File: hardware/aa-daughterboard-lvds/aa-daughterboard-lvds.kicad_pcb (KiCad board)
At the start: 4 copper layers, 112 parts, among them CN1 Barrel_Jack, CN10 6P6C, CN11 6P6C, CN12 6P6C, CN13 6P6C, CN14 Conn_01x08, CN15 Conn_01x08, CN16 Conn_01x08, CN17 8P8C, CN18 8P8C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

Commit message: First run at aa-daughterboard (current loop version), plus WIP
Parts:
- removed C10, C11, C18, C19, C20: 1u, Capacitor_SMD:C_0805_2012Metric
- C12, C13, C14, C6, C7: value 1u -> 0.1u; footprint Capacitor_SMD:C_0805_2012Metric -> Capacitor_SMD:C_0603_1608Metric
- CN10, CN11, CN12, CN13, CN5: footprint aa-daughterboard-lvds:RJ25_Amphenol_90520 -> aa-daughterboard-lvds:6P6C_Assmann_A-2014-1-4
- CN17, CN18, CN19: footprint aa-daughterboard-lvds:RJ25_Assmann_A-2014-2S-4-N-R -> aa-daughterboard-lvds:8P8C_Assmann_A-2014-2S-4
- D6: moved to B.Cu
- moved C15 343.0 mm to (-12.2, 302.4)
- moved C12 343.0 mm to (-12.7, 308.1)
- moved C6 324.4 mm to (71.7, 300.0)
- moved CN15 320.7 mm to (-0.51, 227.8)
- moved CN16 320.2 mm to (-32.5, 202.4)
- moved CN14 320.0 mm to (6.60, 281.7)
- moved U7 309.0 mm to (-12.5, 238.6)
- moved U4 307.5 mm to (70.6, 290.8)
- moved CN5 292.7 mm to (19.1, 74.7), turned to 270 degrees
- moved TP8 290.1 mm to (140.2, 129.0)
- moved D15 289.8 mm to (-5.08, 296.9)
- moved D14 284.6 mm to (-3.81, 285.0)
- moved D16 283.8 mm to (-43.6, 241.0)
- moved C16 274.9 mm to (-43.3, 233.2)
- moved TP7 268.8 mm to (126.7, 130.6)
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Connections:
- CN10 pad 1: GND -> +5V
- CN11 pad 1: GND -> +5V
- CN12 pad 1: GND -> +5V
- CN13 pad 1: GND -> +5V
- CN17 pad 1: Net-(CN14-Pad7) -> Net-(CN14-Pad6)
- CN17 pad 2: Net-(CN14-Pad8) -> Net-(CN14-Pad5)
- CN17 pad 3: Net-(CN14-Pad3) -> Net-(CN14-Pad4)
- CN17 pad 4: Net-(CN14-Pad4) -> Net-(CN14-Pad2)
- CN17 pad 6: Net-(CN14-Pad2) -> Net-(CN14-Pad3)
- CN17 pad 7: Net-(CN14-Pad5) -> Net-(CN14-Pad8)
- CN17 pad 8: Net-(CN14-Pad6) -> Net-(CN14-Pad7)
- CN18 pad 1: Net-(CN15-Pad7) -> Net-(CN15-Pad6)
- CN18 pad 2: Net-(CN15-Pad8) -> Net-(CN15-Pad5)
- CN18 pad 3: Net-(CN15-Pad3) -> Net-(CN15-Pad4)
- CN18 pad 4: Net-(CN15-Pad4) -> Net-(CN15-Pad2)
- CN18 pad 6: Net-(CN15-Pad2) -> Net-(CN15-Pad3)
- CN18 pad 7: Net-(CN15-Pad5) -> Net-(CN15-Pad8)
- CN18 pad 8: Net-(CN15-Pad6) -> Net-(CN15-Pad7)
- CN19 pad 1: Net-(CN16-Pad7) -> Net-(CN16-Pad6)
- CN19 pad 2: Net-(CN16-Pad8) -> Net-(CN16-Pad5)
- CN19 pad 3: Net-(CN16-Pad3) -> Net-(CN16-Pad4)
- CN19 pad 4: Net-(CN16-Pad4) -> Net-(CN16-Pad2)
- CN19 pad 6: Net-(CN16-Pad2) -> Net-(CN16-Pad3)
- CN19 pad 7: Net-(CN16-Pad5) -> Net-(CN16-Pad8)
- CN19 pad 8: Net-(CN16-Pad6) -> Net-(CN16-Pad7)
- CN6 pad 1: Net-(CN10-Pad4) -> Net-(CN10-Pad3)
- CN6 pad 2: Net-(CN10-Pad5) -> Net-(CN10-Pad4)
- CN6 pad 4: Net-(CN10-Pad3) -> Net-(CN10-Pad5)
- CN7 pad 1: Net-(CN11-Pad4) -> Net-(CN11-Pad3)
- CN7 pad 2: Net-(CN11-Pad5) -> Net-(CN11-Pad4)
- CN7 pad 4: Net-(CN11-Pad3) -> Net-(CN11-Pad5)
- CN8 pad 1: Net-(CN12-Pad4) -> Net-(CN12-Pad3)
- CN8 pad 2: Net-(CN12-Pad5) -> Net-(CN12-Pad4)
- CN8 pad 4: Net-(CN12-Pad3) -> Net-(CN12-Pad5)
- CN9 pad 1: Net-(CN13-Pad4) -> Net-(CN13-Pad3)
- CN9 pad 2: Net-(CN13-Pad5) -> Net-(CN13-Pad4)
- CN9 pad 4: Net-(CN13-Pad3) -> Net-(CN13-Pad5)
- D10 pad 3: Net-(CN10-Pad3) -> Net-(CN10-Pad5)
- D10 pad 4: Net-(CN10-Pad4) -> Net-(CN10-Pad3)
- D10 pad 6: Net-(CN10-Pad5) -> Net-(CN10-Pad4)
- D11 pad 3: Net-(CN11-Pad3) -> Net-(CN11-Pad5)
- D11 pad 4: Net-(CN11-Pad4) -> Net-(CN11-Pad3)
- D11 pad 6: Net-(CN11-Pad5) -> Net-(CN11-Pad4)
- D12 pad 3: Net-(CN12-Pad3) -> Net-(CN12-Pad5)
- D12 pad 4: Net-(CN12-Pad4) -> Net-(CN12-Pad3)
- D12 pad 6: Net-(CN12-Pad5) -> Net-(CN12-Pad4)
- D13 pad 3: Net-(CN13-Pad3) -> Net-(CN13-Pad5)
- D13 pad 4: Net-(CN13-Pad4) -> Net-(CN13-Pad3)
- D13 pad 6: Net-(CN13-Pad5) -> Net-(CN13-Pad4)
- R11 pad 1: Net-(D7-Pad1) -> GND
- R11 pad 2: GND -> Net-(D7-Pad1)
- R13 pad 1: Net-(D8-Pad1) -> GND
- R13 pad 2: GND -> Net-(D8-Pad1)
- R14 pad 1: Net-(D9-Pad1) -> GND
- R14 pad 2: GND -> Net-(D9-Pad1)
- R2 pad 1: Net-(D1-Pad1) -> GND
- R2 pad 2: GND -> Net-(D1-Pad1)
- R8 pad 1: Net-(D4-Pad1) -> GND
- R8 pad 2: GND -> Net-(D4-Pad1)
- R9 pad 1: Net-(D5-Pad1) -> GND
- R9 pad 2: GND -> Net-(D5-Pad1)
- U4 pad 10: Net-(CN11-Pad4) -> Net-(CN11-Pad3)
- U4 pad 11: Net-(CN11-Pad5) -> Net-(CN11-Pad4)
- U4 pad 13: Net-(CN11-Pad3) -> Net-(CN11-Pad5)
- U4 pad 2: Net-(CN10-Pad4) -> Net-(CN10-Pad3)
- U4 pad 3: Net-(CN10-Pad5) -> Net-(CN10-Pad4)
- U4 pad 5: Net-(CN10-Pad3) -> Net-(CN10-Pad5)
- U5 pad 10: Net-(CN13-Pad4) -> Net-(CN13-Pad3)
- U5 pad 11: Net-(CN13-Pad5) -> Net-(CN13-Pad4)
- U5 pad 13: Net-(CN13-Pad3) -> Net-(CN13-Pad5)
- U5 pad 2: Net-(CN12-Pad4) -> Net-(CN12-Pad3)
- U5 pad 3: Net-(CN12-Pad5) -> Net-(CN12-Pad4)
- U5 pad 5: Net-(CN12-Pad3) -> Net-(CN12-Pad5)

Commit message: Rough grouping of components done
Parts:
- added R16: 56, Resistor_SMD:R_0603_1608Metric, F.Cu at (86.1, 100.9)
- added R17: 56, Resistor_SMD:R_0603_1608Metric, F.Cu at (80.0, 100.8)
- added R18: 56, Resistor_SMD:R_0603_1608Metric, F.Cu at (79.2, 112.5)
- added R19: 56, Resistor_SMD:R_0603_1608Metric, F.Cu at (84.8, 112.5)
- added R20: 56, Resistor_SMD:R_0603_1608Metric, F.Cu at (84.8, 80.5)
- added R21: 56, Resistor_SMD:R_0603_1608Metric, F.Cu at (79.2, 80.5)
- added R22: 56, Resistor_SMD:R_0603_1608Metric, F.Cu at (78.0, 92.2)
- added R23: 56, Resistor_SMD:R_0603_1608Metric, F.Cu at (83.6, 92.2)
- added R24: 56, Resistor_SMD:R_0603_1608Metric, F.Cu at (84.3, 100.8)
- added R25: 56, Resistor_SMD:R_0603_1608Metric, F.Cu at (82.0, 100.8)
- added R26: 56, Resistor_SMD:R_0603_1608Metric, F.Cu at (81.0, 112.5)
- added R27: 56, Resistor_SMD:R_0603_1608Metric, F.Cu at (83.1, 112.5)
- added R28: 56, Resistor_SMD:R_0603_1608Metric, F.Cu at (83.1, 80.5)
- added R29: 56, Resistor_SMD:R_0603_1608Metric, F.Cu at (81.0, 80.5)
- added R30: 56, Resistor_SMD:R_0603_1608Metric, F.Cu at (79.8, 92.2)
- added R31: 56, Resistor_SMD:R_0603_1608Metric, F.Cu at (81.8, 92.2)
- added R32: 56, Resistor_SMD:R_0603_1608Metric, F.Cu at (84.6, 60.2)
- added R33: 56, Resistor_SMD:R_0603_1608Metric, F.Cu at (79.0, 60.2)
- added R34: 56, Resistor_SMD:R_0603_1608Metric, F.Cu at (78.0, 71.9)
- added R35: 56, Resistor_SMD:R_0603_1608Metric, F.Cu at (83.6, 71.9)
- added R36: 56, Resistor_SMD:R_0603_1608Metric, F.Cu at (64.5, 65.3)
- added R37: 56, Resistor_SMD:R_0603_1608Metric, F.Cu at (58.8, 65.3)
- added R38: 56, Resistor_SMD:R_0603_1608Metric, F.Cu at (57.7, 77.0)
- added R39: 56, Resistor_SMD:R_0603_1608Metric, F.Cu at (63.2, 77.0)
- added R40: 56, Resistor_SMD:R_0603_1608Metric, F.Cu at (64.5, 88.1)
- added R41: 56, Resistor_SMD:R_0603_1608Metric, F.Cu at (58.7, 88.1)
- added R42: 56, Resistor_SMD:R_0603_1608Metric, F.Cu at (57.7, 99.8)
- added R43: 56, Resistor_SMD:R_0603_1608Metric, F.Cu at (63.2, 99.8)
- added R44: 56, Resistor_SMD:R_0603_1608Metric, F.Cu at (82.8, 60.2)
- added R45: 56, Resistor_SMD:R_0603_1608Metric, F.Cu at (80.8, 60.2)
- added R46: 56, Resistor_SMD:R_0603_1608Metric, F.Cu at (79.8, 71.9)
- added R47: 56, Resistor_SMD:R_0603_1608Metric, F.Cu at (81.8, 71.9)
- added R48: 56, Resistor_SMD:R_0603_1608Metric, F.Cu at (62.7, 65.3)
- added R49: 56, Resistor_SMD:R_0603_1608Metric, F.Cu at (60.5, 65.3)
- added R50: 56, Resistor_SMD:R_0603_1608Metric, F.Cu at (59.4, 77.0)
- added R51: 56, Resistor_SMD:R_0603_1608Metric, F.Cu at (61.5, 77.0)
- added R52: 56, Resistor_SMD:R_0603_1608Metric, F.Cu at (62.7, 88.1)
- added R53: 56, Resistor_SMD:R_0603_1608Metric, F.Cu at (60.5, 88.1)
- added R54: 56, Resistor_SMD:R_0603_1608Metric, F.Cu at (59.4, 99.8)
- added R55: 56, Resistor_SMD:R_0603_1608Metric, F.Cu at (61.5, 99.8)
- C2, C8, C9, D10, D11, D12, D13: moved to B.Cu
- Q1: footprint Package_TO_SOT_THT:TO-220-3_Horizontal_TabDown -> Package_TO_SOT_THT:TO-220-3_Vertical
- moved CN17 293.5 mm to (169.7, 90.2)
- moved C15 287.3 mm to (174.2, 83.8), turned to 90 degrees
- moved D15 276.1 mm to (170.4, 83.8)
- moved D14 271.2 mm to (178.1, 83.8), turned to 180 degrees
- moved C12 255.8 mm to (85.6, 71.9), turned to 270 degrees
- moved CN14 254.3 mm to (184.9, 100.3), turned to 180 degrees
- moved D16 253.6 mm to (155.4, 83.8), turned to 180 degrees
- moved CN11 253.1 mm to (173.2, 59.2), turned to 0 degrees
- moved C16 245.5 mm to (151.6, 83.8), turned to 90 degrees
- moved U6 245.5 mm to (81.3, 66.0), turned to 270 degrees
- moved CN18 237.8 mm to (146.8, 90.2), turned to 0 degrees
- moved D11 234.4 mm to (156.5, 54.0), turned to 180 degrees
- moved CN10 232.0 mm to (155.4, 59.2)
- moved D17 229.9 mm to (147.8, 83.8), turned to 180 degrees
- moved C8 229.2 mm to (153.2, 54.0), turned to 270 degrees
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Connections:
- U4 pad 10: Net-(CN11-Pad3) -> Net-(R18-Pad1)
- U4 pad 11: Net-(CN11-Pad4) -> Net-(R26-Pad1)
- U4 pad 13: Net-(CN11-Pad5) -> Net-(R27-Pad1)
- U4 pad 14: Net-(CN11-Pad2) -> Net-(R19-Pad1)
- U4 pad 2: Net-(CN10-Pad3) -> Net-(R16-Pad1)
- U4 pad 3: Net-(CN10-Pad4) -> Net-(R24-Pad1)
- U4 pad 5: Net-(CN10-Pad5) -> Net-(R25-Pad1)
- U4 pad 6: Net-(CN10-Pad2) -> Net-(R17-Pad1)
- U5 pad 10: Net-(CN13-Pad3) -> Net-(R22-Pad1)
- U5 pad 11: Net-(CN13-Pad4) -> Net-(R30-Pad1)
- U5 pad 13: Net-(CN13-Pad5) -> Net-(R31-Pad1)
- U5 pad 14: Net-(CN13-Pad2) -> Net-(R23-Pad1)
- U5 pad 2: Net-(CN12-Pad3) -> Net-(R20-Pad1)
- U5 pad 3: Net-(CN12-Pad4) -> Net-(R28-Pad1)
- U5 pad 5: Net-(CN12-Pad5) -> Net-(R29-Pad1)
- U5 pad 6: Net-(CN12-Pad2) -> Net-(R21-Pad1)
- U6 pad 10: Net-(CN14-Pad5) -> Net-(R34-Pad1)
- U6 pad 11: Net-(CN14-Pad6) -> Net-(R46-Pad1)
- U6 pad 13: Net-(CN14-Pad8) -> Net-(R47-Pad1)
- U6 pad 14: Net-(CN14-Pad7) -> Net-(R35-Pad1)
- U6 pad 2: Net-(CN14-Pad1) -> Net-(R32-Pad1)
- U6 pad 3: Net-(CN14-Pad2) -> Net-(R44-Pad1)
- U6 pad 5: Net-(CN14-Pad4) -> Net-(R45-Pad1)
- U6 pad 6: Net-(CN14-Pad3) -> Net-(R33-Pad1)
- U7 pad 10: Net-(CN15-Pad5) -> Net-(R38-Pad1)
- U7 pad 11: Net-(CN15-Pad6) -> Net-(R50-Pad1)
- U7 pad 13: Net-(CN15-Pad8) -> Net-(R51-Pad1)
- U7 pad 14: Net-(CN15-Pad7) -> Net-(R39-Pad1)
- U7 pad 2: Net-(CN15-Pad1) -> Net-(R36-Pad1)
- U7 pad 3: Net-(CN15-Pad2) -> Net-(R48-Pad1)
- U7 pad 5: Net-(CN15-Pad4) -> Net-(R49-Pad1)
- U7 pad 6: Net-(CN15-Pad3) -> Net-(R37-Pad1)
- U8 pad 10: Net-(CN16-Pad5) -> Net-(R42-Pad1)
- U8 pad 11: Net-(CN16-Pad6) -> Net-(R54-Pad1)
- U8 pad 13: Net-(CN16-Pad8) -> Net-(R55-Pad1)
- U8 pad 14: Net-(CN16-Pad7) -> Net-(R43-Pad1)
- U8 pad 2: Net-(CN16-Pad1) -> Net-(R40-Pad1)
- U8 pad 3: Net-(CN16-Pad2) -> Net-(R52-Pad1)
- U8 pad 5: Net-(CN16-Pad4) -> Net-(R53-Pad1)
- U8 pad 6: Net-(CN16-Pad3) -> Net-(R41-Pad1)

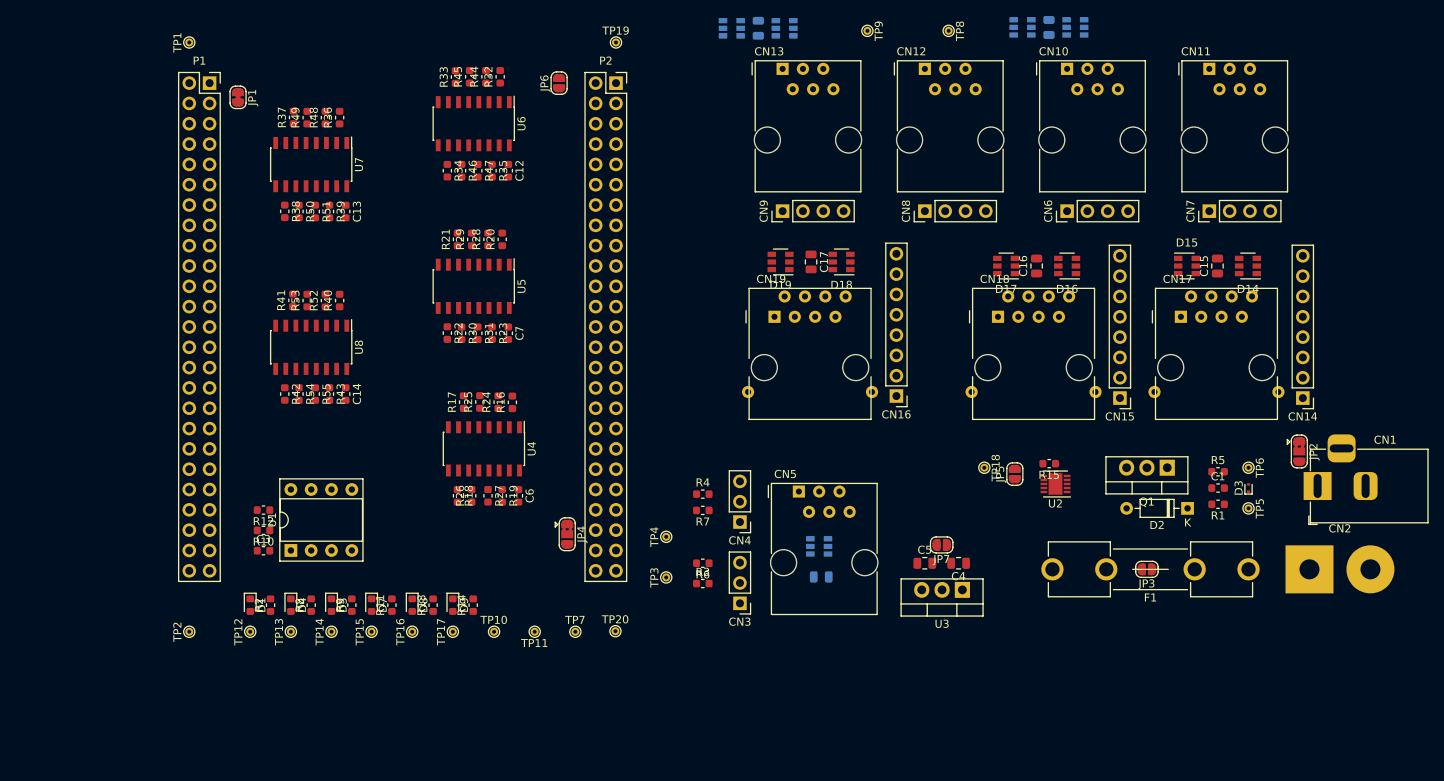
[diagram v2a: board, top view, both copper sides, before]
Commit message: Add STM32 symbols... I don't think I have this right yet
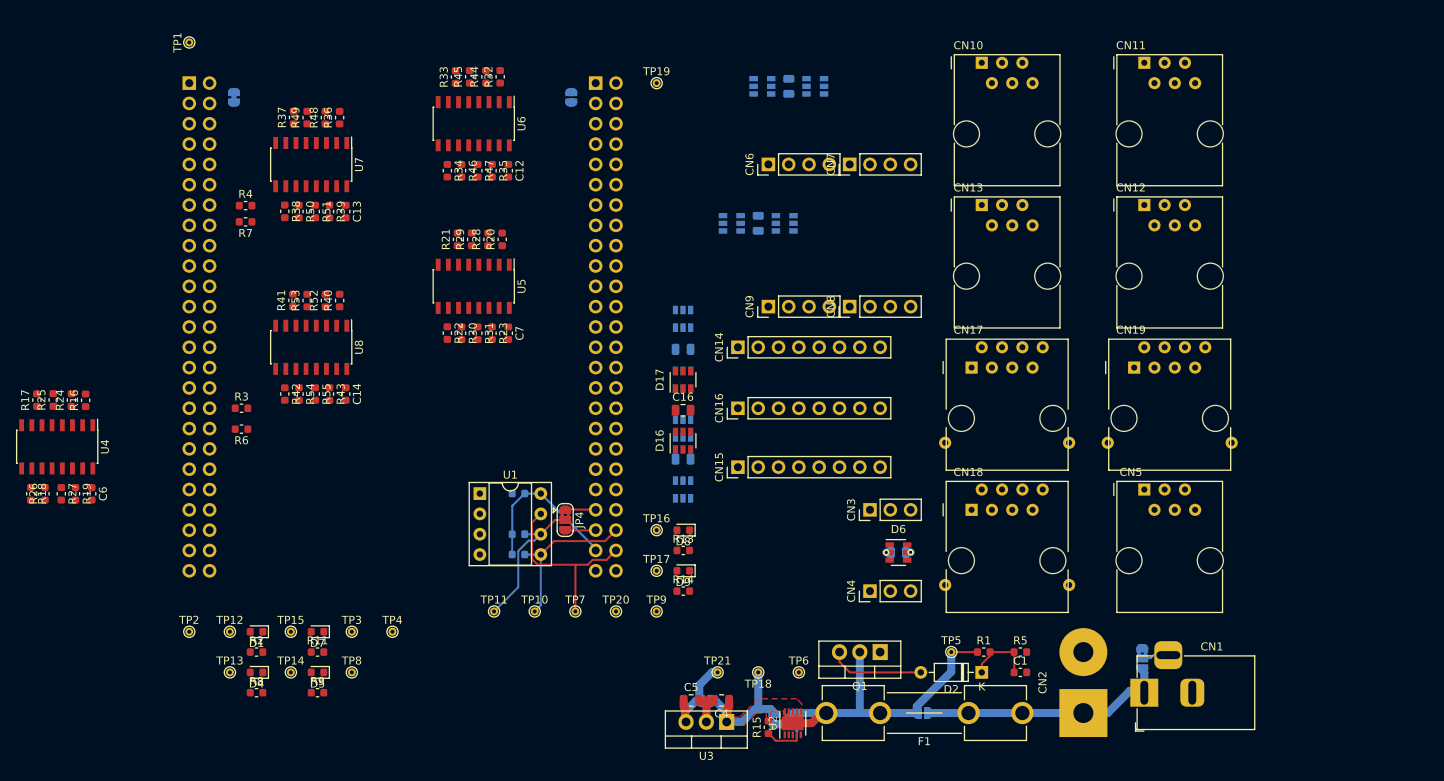
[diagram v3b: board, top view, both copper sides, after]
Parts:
- added TP21: TestPoint, TestPoint:TestPoint_THTPad_D1.0mm_Drill0.5mm, F.Cu at (111.8, 134.6)
- C15, C17, C3, D14, D15, D18, D19, D3, JP1, JP2, JP3, JP5, JP6, JP7, P1, P2, R10, R12: moved to B.Cu
- D6: moved to F.Cu
- moved TP8 109.5 mm to (66.0, 134.6), turned to 0 degrees
- moved TP9 77.2 mm to (104.1, 127.0), turned to 0 degrees
- moved D14 72.0 mm to (107.4, 98.0), turned to 90 degrees
- moved CN14 70.9 mm to (114.3, 94.0), turned to 90 degrees
- moved C15 67.6 mm to (107.4, 94.2), turned to 180 degrees
- moved R4 67.6 mm to (52.8, 76.3)
- moved R7 67.6 mm to (52.8, 78.3)
- moved D3 63.9 mm to (121.7, 141.5), turned to 270 degrees
- moved D15 63.3 mm to (107.4, 90.4), turned to 270 degrees
- moved TP6 61.8 mm to (121.9, 134.6), turned to 0 degrees
- moved R3 61.7 mm to (52.3, 101.6)
- moved R6 60.0 mm to (52.3, 104.2)
- moved R17 53.3 mm to (26.7, 100.6)
- moved R18 53.3 mm to (25.9, 112.3)
- moved R19 53.3 mm to (31.5, 112.3)
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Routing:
- net Net-(D3-Pad1): track 0.00 -> 43.0 mm
- net Net-(CN1-Pad1): track 0.00 -> 30.8 mm
- net /MEM_WP: track 0.00 -> 23.5 mm
- net /MEM_PWR: track 0.00 -> 20.2 mm
- net /I2C_SDA: track 0.00 -> 20.1 mm
- net /I2C_SCL: track 0.00 -> 18.3 mm
- net VDD: track 0.00 -> 17.8 mm
- net Net-(D2-Pad2): track 0.00 -> 11.9 mm
- net +5V: track 0.00 -> 11.0 mm
- net Net-(C1-Pad1): track 0.00 -> 8.52 mm
- net GND: track 0.00 -> 5.14 mm, vias 0 -> 1
- net Net-(R15-Pad1): track 0.00 -> 4.64 mm
- net /PA8: track 0.00 -> 3.82 mm
- net /PC8: track 0.00 -> 3.78 mm
- net Net-(CN1-Pad3): track 0.00 -> 3.41 mm
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- added copper zone on F.Cu, net VDD
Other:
- net class High Current added: clearance 0.2, trace_width 1, via_dia 0.8, via_drill 0.4
- net class Line Drive Broadside added: clearance 0.2, trace_width 0.5, via_dia 0.8, via_drill 0.4
- net class Line Drive Microstrip added: clearance 0.2, trace_width 0.5, via_dia 0.8, via_drill 0.4
- net class Power added: clearance 0.2, trace_width 1, via_dia 0.8, via_drill 0.4
